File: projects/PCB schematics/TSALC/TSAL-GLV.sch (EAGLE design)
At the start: 27 parts, among them IC2 78L08SMD, IC4 NE555D, Q1 IRLZ44Z, Q2 IRLZ44Z, Q3 IRLZ44Z

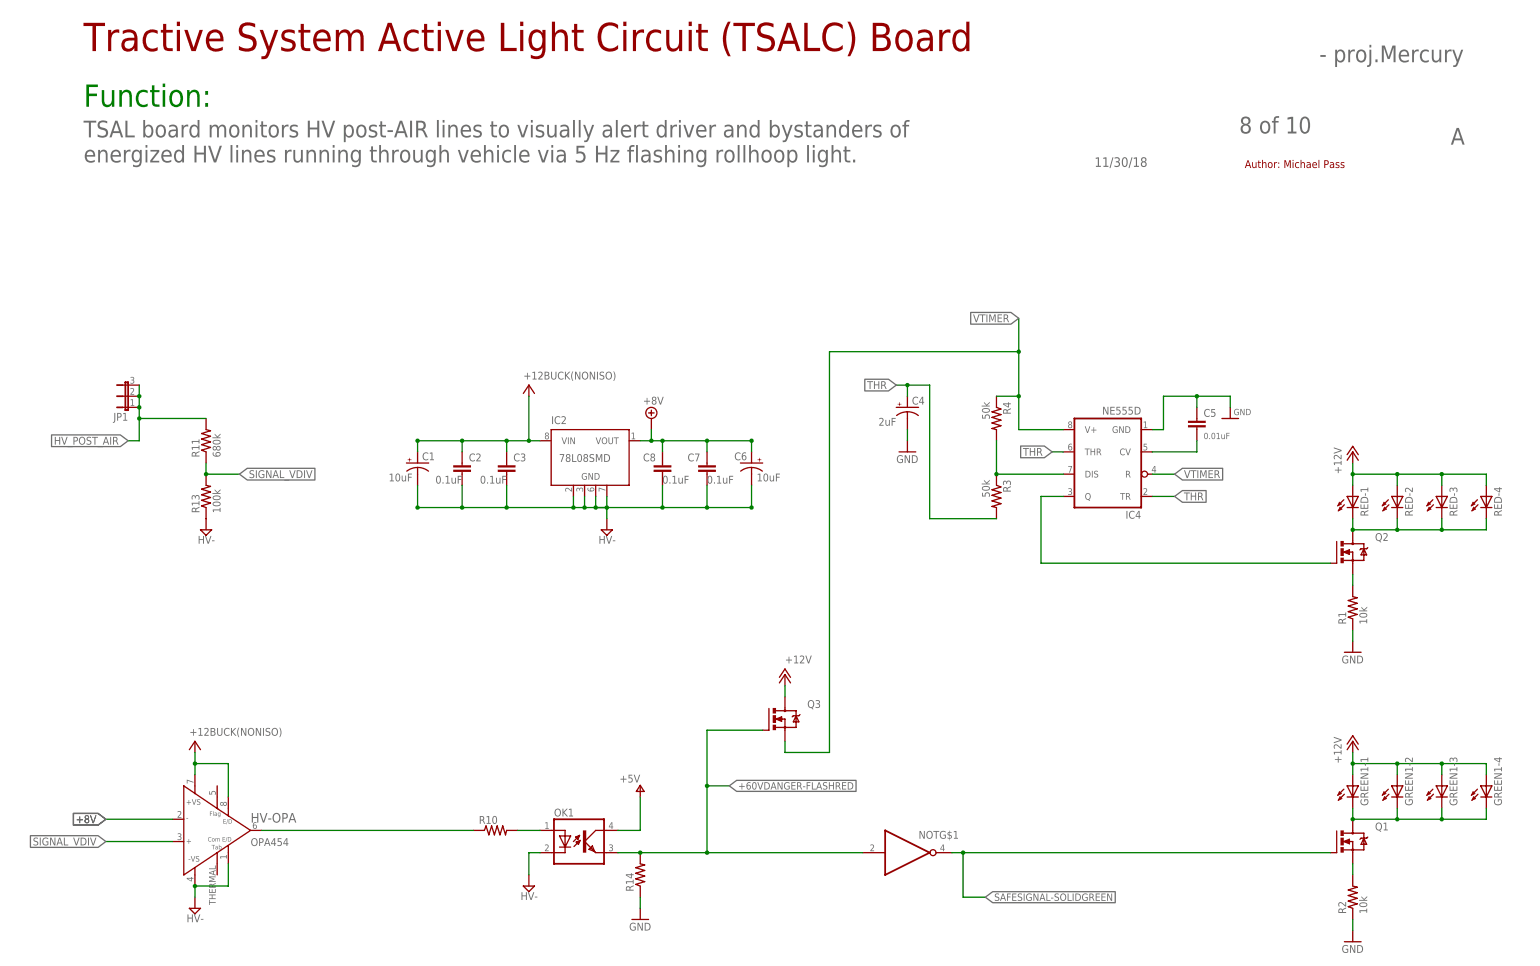
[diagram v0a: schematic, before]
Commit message: TSALC - TS initial revision.
Squash - TSALC - Added current limited resistors to OK1.

Squash - TSALC - Hand routing complete.

GLV components moved over to a separate board with minimal connections left on TS part. Distance explicitly shown on silkscreen. Will require conformal coating to fall in specification.

All high volt connectors are on the top of the board (vertical connectors chosen, as this will occur outside of accumulator container.)

Will tidy silkscreen and check for DRC errors.

Squash - TSALC - Silkscreen additions.

Logo and author addition.
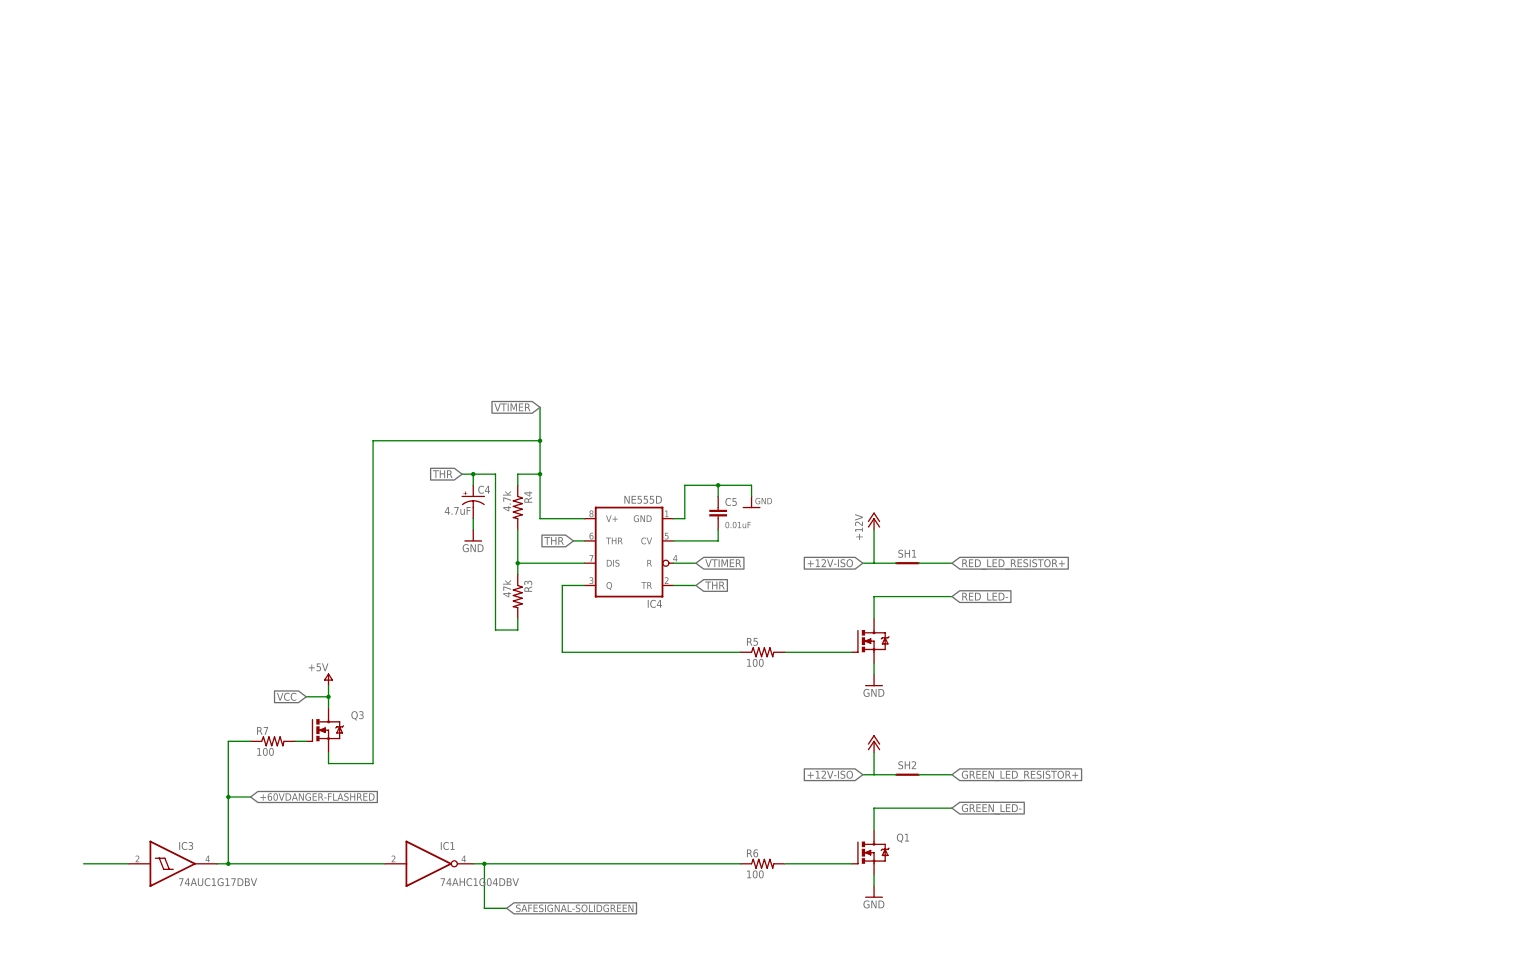
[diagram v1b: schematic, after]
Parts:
- removed C1, C6: 10uF, rcl:CPOL-US085CS-1AW
- removed C2, C3, C7, C8: 0.1uF, rcl:C-EUC0805
- removed GREEN1, RED: LZR184, led:LZR184
- removed HV-OPA: OPA454, OPA454:OPA454
- removed IC2: 78L08SMD, linear:78L08SMD
- removed JP1: (no value), jumper:JP2W
- removed NOT: 74LVC1G06DCK, 74xx-little-us:74LVC1G06DCK
- removed OK1: PC817-S, iowaFormula:PC817-S
- removed R1, R2: 10k, rcl:R-US_R0805
- removed R10, R14: (no value), rcl:R-US_R0805
- removed R11: 680k, rcl:R-US_R0805
- removed R13: 100k, rcl:R-US_R0805
- added IC1: 74AHC1G04DBV, 74xx-little-us:74AHC1G04DBV
- added IC3: 74AUC1G17DBV, 74xx-little-us:74AUC1G17DBV
- added R5, R6, R7: 100, rcl:R-US_R0805
- added SH1, SH2: SHORTT5, shorts:SHORTT5
- C4: value 2uF -> 4.7uF
- R3: value 50k -> 47k
- R4: value 50k -> 4.7k
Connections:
- removed net +12V: GREEN1-1.A, GREEN1-2.A, GREEN1-3.A, GREEN1-4.A, Q3.D, RED-1.A, RED-2.A, RED-3.A, RED-4.A
- removed net +8V: C6.+, C7.1, C8.1, HV-OPA.IN-, IC2G$1.VOUT
- removed net HV-: C1.-, C2.2, C3.2, C6.-, C7.2, C8.2, HV-OPA.-VS, HV-OPA.E/DCOM, IC2G$1.GND@1, IC2G$1.GND@2, IC2G$1.GND@3, IC2G$1.GND@4
- removed net HV_POST_AIR: JP1.1, JP1.2, JP1.3, R11.2
- removed net N$10: OK1.A, R10.2
- removed net N$3: GREEN1-1.C, GREEN1-2.C, GREEN1-3.C, GREEN1-4.C, Q1.D
- removed net N$4: Q1.S, R2.2
- removed net N$5: Q2.D, RED-1.C, RED-2.C, RED-3.C, RED-4.C
- removed net N$6: Q2.S, R1.2
- removed net N$9: HV-OPA.OUT, R10.1
- removed net SIGNAL_VDIV: HV-OPA.IN+, R11.1, R13.2
- removed net V+: C1.+, C2.1, C3.1, HV-OPA.+VS, HV-OPA.E/D, IC2G$1.VIN, OK1.COL
- new net +12V-ISO: SH1.P$1, SH2.P$1
- new net GREEN_LED-: Q1.D
- new net GREEN_LED_RESISTOR+: SH2.P$2
- new net N$1: IC4.Q, R5.1
- new net N$11: Q3.G, R7.2
- new net N$13: IC3G$1.I
- new net N$14: Q1.G, R6.2
- new net RED_LED-: Q2.D
- new net RED_LED_RESISTOR+: SH1.P$2
- new net VCC: Q3.D
- net +60VDANGER-FLASHRED: now also IC1A.I, IC3G$1.O, R7.1; no longer NOTG$1.I, OK1.EMIT, Q3.G, R14.2
- net GND: now also Q1.S, Q2.S; no longer OK1.C, R1.1, R13.1, R14.1, R2.1
- net N$8: now also R5.2; no longer IC4.Q
- net SAFESIGNAL-SOLIDGREEN: now also IC1A.O, R6.1; no longer NOTG$1.O, Q1.G
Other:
- note added: "EV.6.10.3 When the voltage outside the accumulator container(s) exceeds 60 V DC or 25 V AC RMS, the TSAL must: a. Be Color: Red b. Flash continuously with a frequency between 2 Hz and 5 Hz"
- note removed: "- proj.Mercury"
- note removed: "11/30/18"
- note removed: "8 of 10"
- note removed: "A"
- note removed: "Author: Michael Pass"
- note removed: "Formula"
- note removed: "Function:"
- note removed: "Iowa"
- note removed: "TSAL board monitors HV post-AIR lines to visually alert driver and bystanders of energized HV lines running through vehicle via 5 Hz flashing rollhoop light."
- note removed: "Tractive System Active Light Circuit (TSALC) Board"
- moved on the sheet: C4, C5, IC4, Q1, Q3, R3, R4

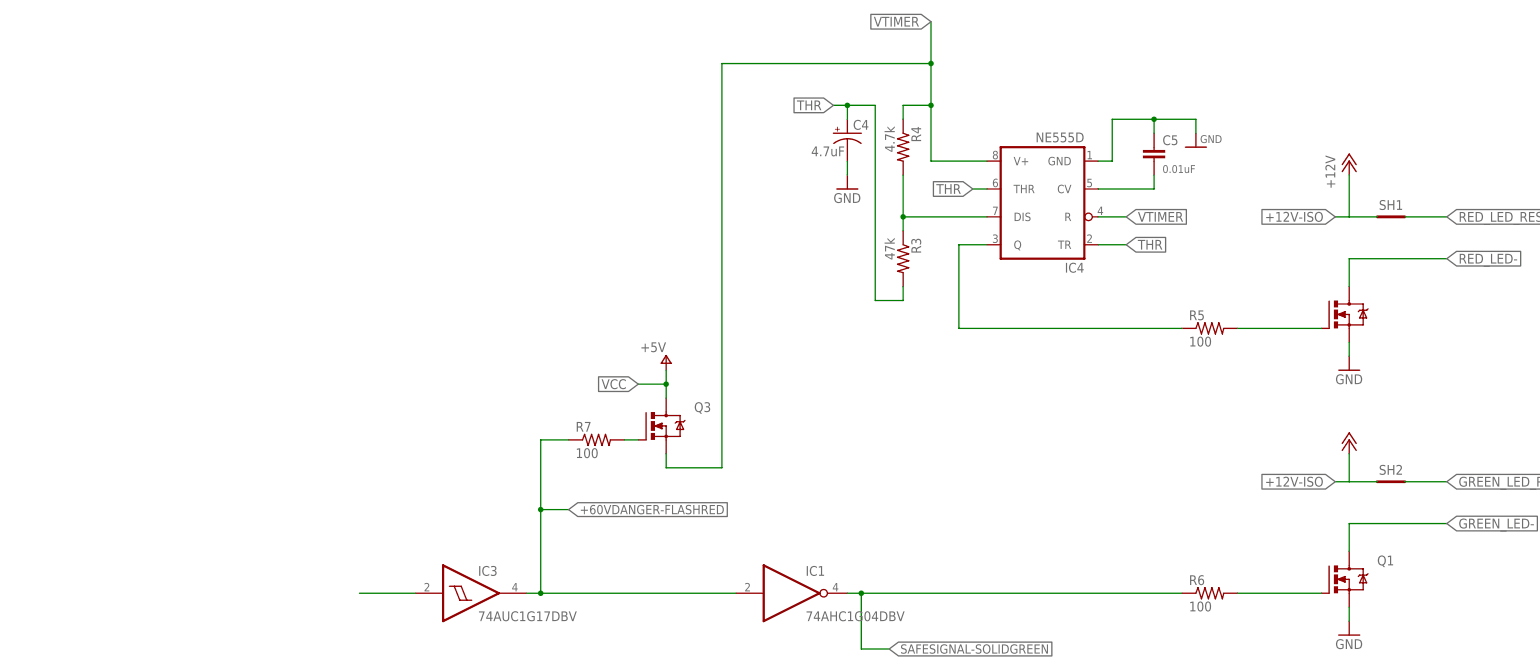
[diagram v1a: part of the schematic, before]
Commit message: TSALC - GLV board completed.
Preliminary layout completed for GLV. Must silkscreen and double check connections between GLV and TS boards.

Squash - TSALC - Silkscreen additions.
Initial silkscreen work done. Inputs and outputs must be annotated.
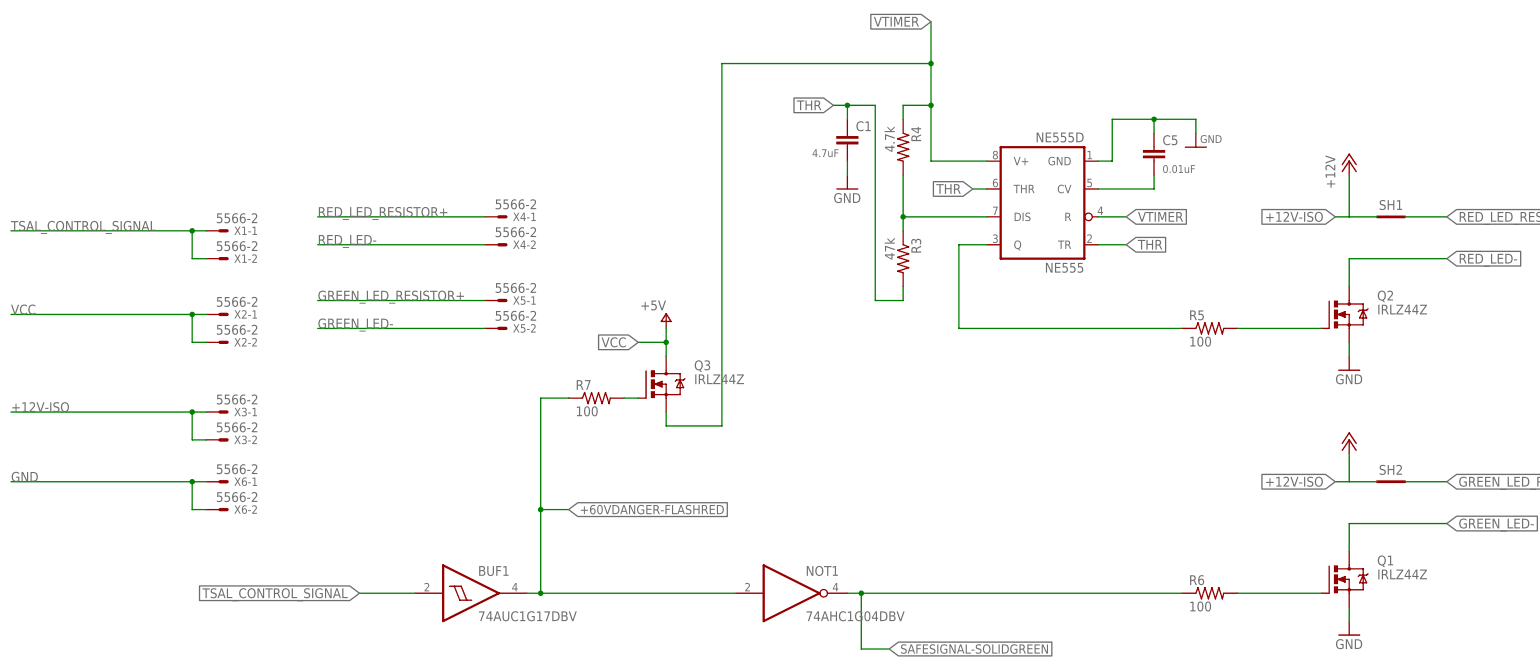
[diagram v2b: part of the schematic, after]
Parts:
- removed C4: 4.7uF, rcl:CPOL-US085CS-1AW
- added C1: 4.7uF, rcl:C-EUC0805
- added X1, X2, X3, X4, X5, X6: 5566-2, con-molex:5566-2
- renumbered IC1 to NOT1, IC3 to BUF1, IC4 to NE555
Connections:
- removed net N$13: BUF1G$1.I
- new net TSAL_CONTROL_SIGNAL: BUF1G$1.I, X1-1.S, X1-2.S
- net +12V-ISO: now also X3-1.S, X3-2.S
- net GND: now also C1.2, X6-1.S, X6-2.S; no longer C4.-
- net GREEN_LED-: now also X5-2.S
- net GREEN_LED_RESISTOR+: now also X5-1.S
- net RED_LED-: now also X4-2.S
- net RED_LED_RESISTOR+: now also X4-1.S
- net THR: now also C1.1; no longer C4.+
- net VCC: now also X2-1.S, X2-2.S
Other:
- moved on the sheet: Q3, R7

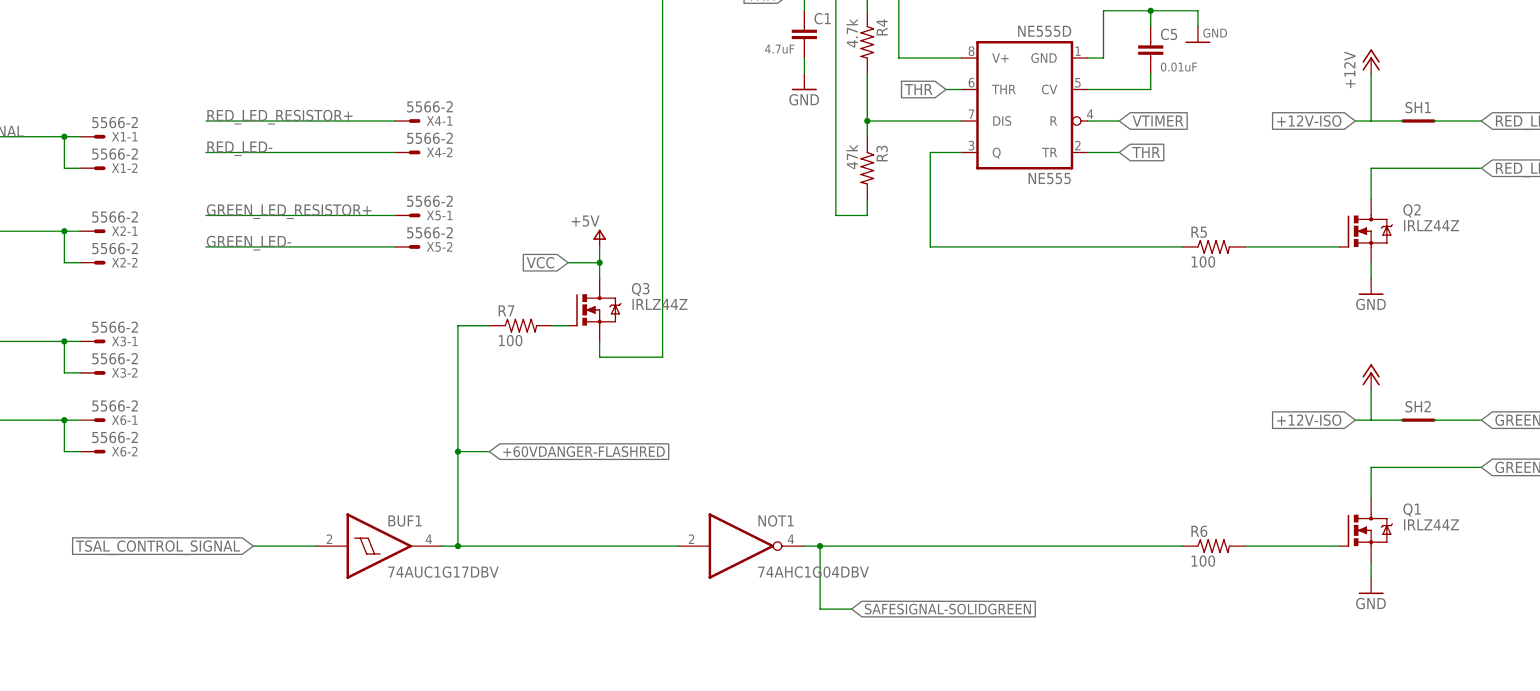
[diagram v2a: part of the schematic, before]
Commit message: TSALC - GLV; Rev A.
GLV ready for pull request review.
This board has nothing but GLV components on it.
Interface to TS board occurs between VCC and TSAL_CONTROL_SIGNAL

Squash - TSALC - GLV; Added pull-down resistor to input.
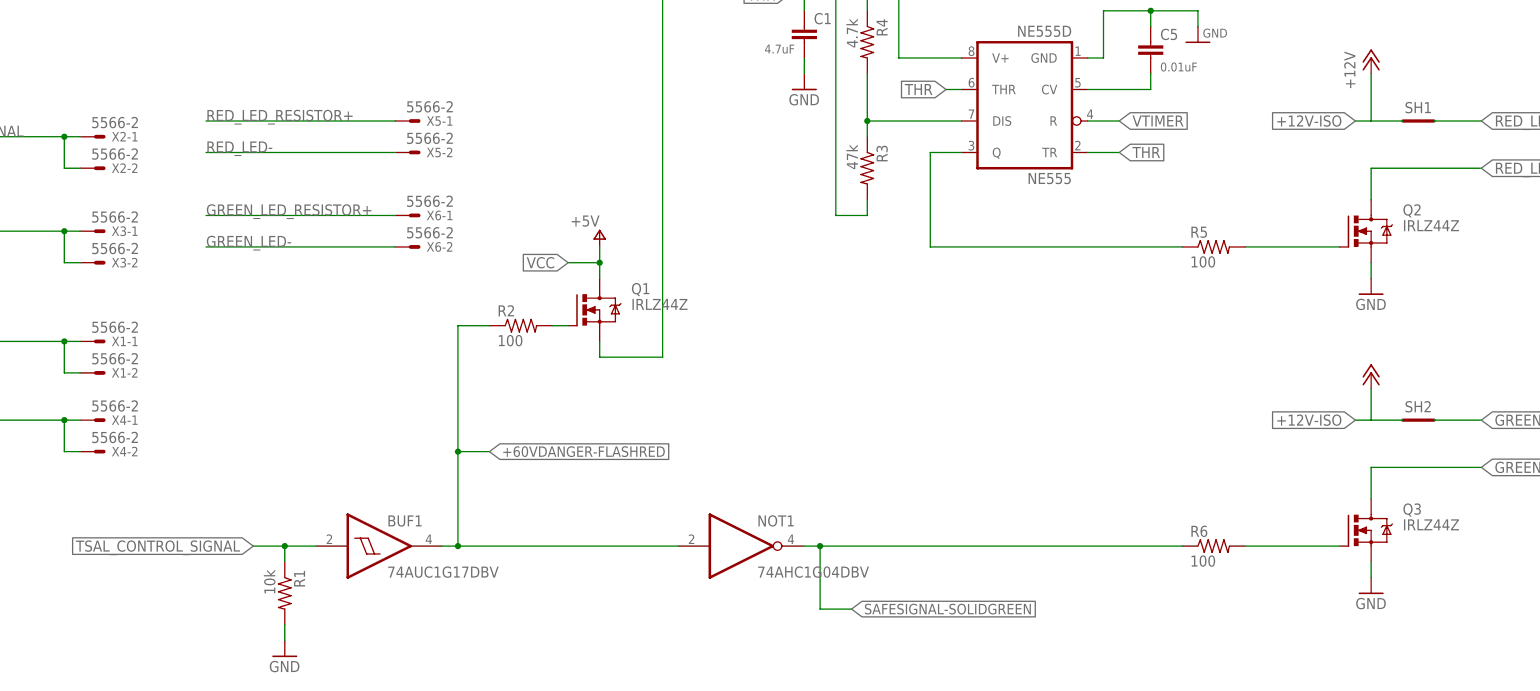
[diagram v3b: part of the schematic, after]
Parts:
- added R1: 10k, rcl:R-US_R0805
- renumbered R7 to R2
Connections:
- net +12V-ISO: now also X1-1.S, X1-2.S; no longer X3-1.S, X3-2.S
- net GND: now also Q3.S, R1.2, X4-1.S, X4-2.S; no longer Q1.S, X6-1.S, X6-2.S
- net GREEN_LED-: now also Q3.D, X6-2.S; no longer Q1.D, X5-2.S
- net GREEN_LED_RESISTOR+: now also X6-1.S; no longer X5-1.S
- net N$11: now also Q1.G; no longer Q3.G
- net N$14: now also Q3.G; no longer Q1.G
- net RED_LED-: now also X5-2.S; no longer X4-2.S
- net RED_LED_RESISTOR+: now also X5-1.S; no longer X4-1.S
- net TSAL_CONTROL_SIGNAL: now also R1.1, X2-1.S, X2-2.S; no longer X1-1.S, X1-2.S
- net VCC: now also Q1.D, X3-1.S, X3-2.S; no longer Q3.D, X2-1.S, X2-2.S
- net VTIMER: now also Q1.S; no longer Q3.S
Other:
- moved on the sheet: Q1, Q3, X1-1, X1-2, X2-1, X2-2, X3-1, X3-2, X4-1, X4-2, X5-1, X5-2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

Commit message: PROJ - Final pre-purchase revisions (4 boards still in progress.)
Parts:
- removed X1, X2, X3, X4, X5, X6: 5566-2, con-molex:5566-2
- added +12V-ISO.1, GND.1, GREEN_LED, RED_LED, TSAL_CONTROL_SIGNAL, VCC.1: 5566-2, con-molex:5566-2
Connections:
- net +12V-ISO: now also +12V-ISO.1-1.S, +12V-ISO.1-2.S; no longer X1-1.S, X1-2.S
- net GND: now also GND.1-1.S, GND.1-2.S; no longer X4-1.S, X4-2.S
- net GREEN_LED-: now also GREEN_LED-2.S; no longer X6-2.S
- net GREEN_LED_RESISTOR+: now also GREEN_LED-1.S; no longer X6-1.S
- net RED_LED-: now also RED_LED-2.S; no longer X5-2.S
- net RED_LED_RESISTOR+: now also RED_LED-1.S; no longer X5-1.S
- net TSAL_CONTROL_SIGNAL: now also TSAL_CONTROL_SIGNAL-1.S, TSAL_CONTROL_SIGNAL-2.S; no longer X2-1.S, X2-2.S
- net VCC: now also VCC.1-1.S, VCC.1-2.S; no longer X3-1.S, X3-2.S
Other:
- moved on the sheet: BUF1, C1, C5, NE555, NOT1, Q1, Q2, Q3, R1, R2, R3, R4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
